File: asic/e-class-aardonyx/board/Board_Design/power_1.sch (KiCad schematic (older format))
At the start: 28 parts, among them J5 PJ-202H PWRJACK, J6 Conn_1x3_M, SW1 SW_SPST, U4 TPS54627DDAR

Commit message: update pending  footprint
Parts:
- F1: footprint Capacitor_THT:C_Disc_D9.0mm_W5.0mm_P7.50mm -> Aardonyx:vishay_ptccl_d1mm_w5mm
- SW1: footprint Button_Switch_THT:SW_NKK_G1xJP -> Aardonyx:SW_toggle_spst_2.54mm
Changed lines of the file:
@@
 EESchema Schematic File Version 4
-LIBS:Aardonyx-cache
-EELAYER 29 0
+EELAYER 30 0
 EELAYER END
 $Descr A4 11693 8268
@@
 F 0 "F1" V 4475 1600 50  0000 C CNN
 F 1 "PTCCL13H921DBE" V 4550 1700 50  0000 C CNN
-F 2 "Capacitor_THT:C_Disc_D9.0mm_W5.0mm_P7.50mm" H 4750 1400 50  0001 L CNN
+F 2 "Aardonyx:vishay_ptccl_d1mm_w5mm" H 4750 1400 50  0001 L CNN
 F 3 "https://www.digikey.in/products/en?keywords=PTCCL13H921DBE" H 4700 1600 50  0001 C CNN
 F 4 "PTC RESET FUSE 30V 920MA RADIAL" H 4700 1600 50  0001 C CNN "Description"
@@
 F 0 "SW1" H 4200 1835 50  0000 C CNN
 F 1 "SW_SPST" H 4200 1744 50  0000 C CNN
-F 2 "Button_Switch_THT:SW_NKK_G1xJP" H 4200 1600 50  0001 C CNN
+F 2 "Aardonyx:SW_toggle_spst_2.54mm" H 4200 1600 50  0001 C CNN
 F 3 "https://www.digikey.com/product-detail/en/te-connectivity-alcoswitch-switches/TMS6T1B1M1QE/450-2109-ND/5125729" H 4200 1600 50  0001 C CNN
 F 4 "SWITCH TOGGLE SPST 3A 120V" H 4200 1600 50  0001 C CNN "Description"

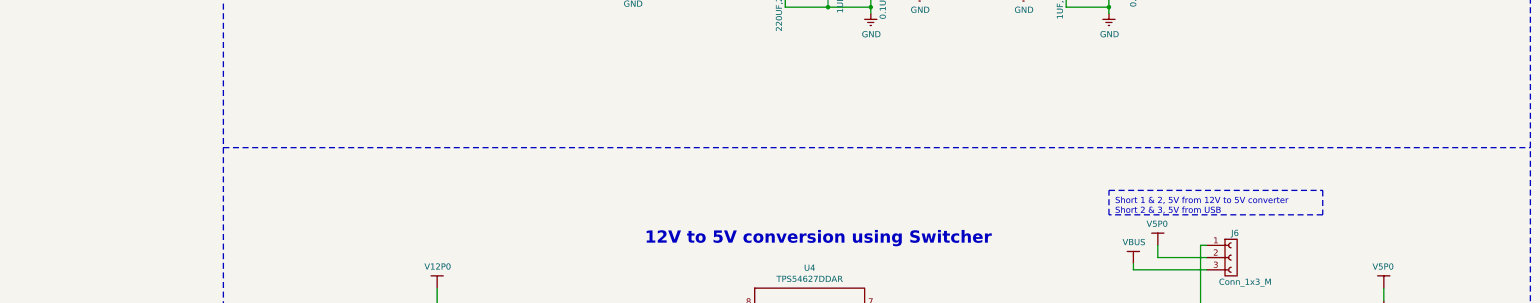
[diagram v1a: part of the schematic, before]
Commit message: update footprint & component placement
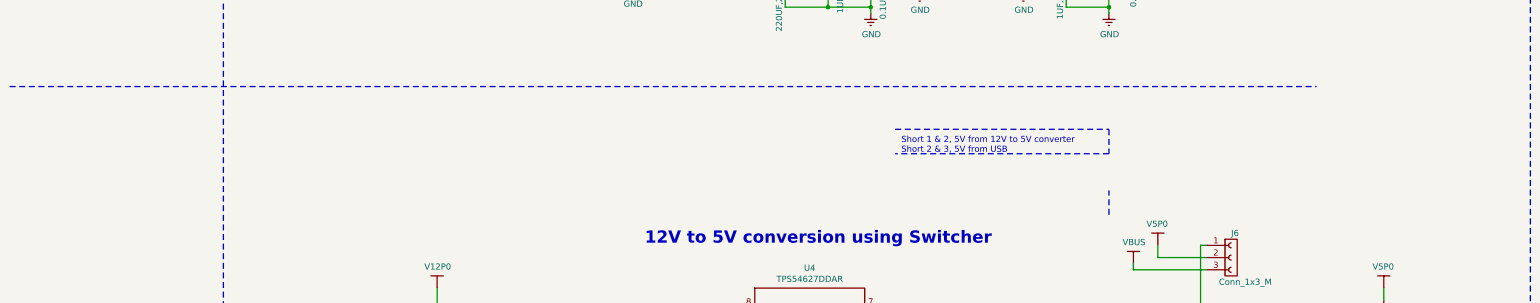
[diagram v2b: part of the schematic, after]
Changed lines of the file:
@@
 	500  7750 500  500
 Wire Notes Line
-	500  3300 11200 3300
+	-1250 2800 9450 2800
 Text Notes 3950 4100 0    100  ~ 20
 12V to 5V conversion using Switcher
@@
 	0    1    1    0
 $EndComp
-Text Notes 7800 3850 0    50   ~ 0
+Text Notes 6050 3350 0    50   ~ 0
 Short 1 & 2, 5V from 12V to 5V converter\nShort 2 & 3, 5V from USB
 $Comp
@@
 $EndComp
 Wire Notes Line
-	7750 3650 9500 3650
+	6000 3150 7750 3150
 Wire Notes Line
-	9500 3650 9500 3850
+	7750 3150 7750 3350
 Wire Notes Line
-	9500 3850 7750 3850
+	7750 3350 6000 3350
 Wire Notes Line
 	7750 3850 7750 3650

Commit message: updated compo placement
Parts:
- TP5: footprint TestPoint:TestPoint_Bridge_Pitch2.54mm_Drill0.7mm -> Connector_PinHeader_2.54mm:PinHeader_1x01_P2.54mm_Vertical
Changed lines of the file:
@@
 F 0 "TP5" V 10104 6238 50  0000 L CNN
 F 1 "TestPoint" V 10195 6238 50  0000 L CNN
-F 2 "TestPoint:TestPoint_Bridge_Pitch2.54mm_Drill0.7mm" H 10350 6050 50  0001 C CNN
+F 2 "Connector_PinHeader_2.54mm:PinHeader_1x01_P2.54mm_Vertical" H 10350 6050 50  0001 C CNN
 F 3 "" H 10350 6050 50  0001 C CNN
 	1    10150 6050

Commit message: add bom
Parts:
- C37: Maufaturer AVX Corporation -> AVX Corporation
- D3: Maufaturer Lumex Opto/Components Inc. -> Lumex Opto/Components Inc.
- L1: Description CMC 15A 2LN 60 OHM SMD -> CMC 15A 2LN 60 OHM SMD; Maufaturer Laird-Signal Integrity Products -> Laird-Signal Integrity Products
- SW1: Digikey PartNumber SWITCH TOGGLE SPST 3A 120V -> TMS6T1B1M1QE
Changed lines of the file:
@@
 F 5 "478-12518-1-ND" H 5100 1850 50  0001 C CNN "Digikey PartNumber"
 F 6 "TCN4227M025R0100" H 5100 1850 50  0001 C CNN "Manufactured Part Number"
-F 7 "	AVX Corporation" H 5100 1850 50  0001 C CNN "Maufaturer"
+F 7 "AVX Corporation" H 5100 1850 50  0001 C CNN "Maufaturer"
 	1    5100 1850
 	1    0    0    -1
@@
 F 2 "Aardonyx:L_Laird_L9.55_W2.84" H 6600 1700 50  0001 C CNN
 F 3 "https://www.digikey.com/product-detail/en/laird-signal-integrity-products/CM3421Y600R-10/240-2501-1-ND/935987" H 6600 1700 50  0001 C CNN
-F 4 "	CMC 15A 2LN 60 OHM SMD" H 6600 1700 50  0001 C CNN "Description"
+F 4 "CMC 15A 2LN 60 OHM SMD" H 6600 1700 50  0001 C CNN "Description"
 F 5 "240-2501-1-ND" H 6600 1700 50  0001 C CNN "Digikey PartNumber"
 F 6 "CM3421Y600R-10" H 6600 1700 50  0001 C CNN "Manufactured Part Number"
-F 7 "	Laird-Signal Integrity Products" H 6600 1700 50  0001 C CNN "Maufaturer"
+F 7 "Laird-Signal Integrity Products" H 6600 1700 50  0001 C CNN "Maufaturer"
 	1    6600 1700
 	1    0    0    -1
@@
 F 3 "https://www.digikey.com/product-detail/en/lumex-opto-components-inc/SML-LX1206GW-TR/67-1002-1-ND/270799" H 10000 5150 50  0001 C CNN
 F 4 "LED GREEN DIFFUSED 1206 SMD" H 10000 5150 50  0001 C CNN "Description"
-F 5 "	Lumex Opto/Components Inc." H 10000 5150 50  0001 C CNN "Maufaturer"
+F 5 "Lumex Opto/Components Inc." H 10000 5150 50  0001 C CNN "Maufaturer"
 F 6 "67-1002-1-ND" H 10000 5150 50  0001 C CNN "Digikey PartNumber"
 F 7 "SML-LX1206GW-TR" H 10000 5150 50  0001 C CNN "Manufactured Part Number"
@@
 F 3 "https://www.digikey.com/product-detail/en/te-connectivity-alcoswitch-switches/TMS6T1B1M1QE/450-2109-ND/5125729" H 4200 1600 50  0001 C CNN
 F 4 "SWITCH TOGGLE SPST 3A 120V" H 4200 1600 50  0001 C CNN "Description"
-F 5 "SWITCH TOGGLE SPST 3A 120V" H 4200 1600 50  0001 C CNN "Digikey PartNumber"
+F 5 "TMS6T1B1M1QE" H 4200 1600 50  0001 C CNN "Digikey PartNumber"
 F 6 "TMS6T1B1M1QE (2267080-1)" H 4200 1600 50  0001 C CNN "Manufactured Part Number"
 F 7 "TE Connectivity ALCOSWITCH Switches" H 4200 1600 50  0001 C CNN "Maufaturer"

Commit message: Updated few components
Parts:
- L2: Description FIXED IND 3.3UH 6.6A 17 MOHM SMD -> FIXED IND 3.3UH 6.6A 15 MOHM SMD; Digikey PartNumber 732-6781-2-ND -> SRN8040TA-3R3YCT-ND; Manufactured Part Number 78477033 -> SRN8040TA-3R3Y; Maufaturer Wurth Elektronik -> Bourns Inc.
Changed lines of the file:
@@
 EESchema Schematic File Version 4
-EELAYER 30 0
+LIBS:Aardonyx-cache
+EELAYER 29 0
 EELAYER END
 $Descr A4 11693 8268
@@
 F 1 "3.3UH" V 6600 4900 50  0000 C CNN
 F 2 "Inductor_SMD:L_Wuerth_WE-PD-Typ-LS" H 6650 4900 50  0001 C CNN
-F 3 "https://www.digikey.com/product-detail/en/w%C3%BCrth-elektronik/78477033/732-6781-2-ND/5168775" H 6650 4900 50  0001 C CNN
-F 4 "FIXED IND 3.3UH 6.6A 17 MOHM SMD" H 6650 4900 50  0001 C CNN "Description"
-F 5 "732-6781-2-ND" H 6650 4900 50  0001 C CNN "Digikey PartNumber"
-F 6 "78477033" H 6650 4900 50  0001 C CNN "Manufactured Part Number"
-F 7 "Wurth Elektronik" H 6650 4900 50  0001 C CNN "Maufaturer"
+F 3 "https://www.digikey.in/product-detail/en/bourns-inc/SRN8040TA-3R3Y/SRN8040TA-3R3YCT-ND/6155255" H 6650 4900 50  0001 C CNN
+F 4 "	FIXED IND 3.3UH 6.6A 15 MOHM SMD" H 6650 4900 50  0001 C CNN "Description"
+F 5 "SRN8040TA-3R3YCT-ND" H 6650 4900 50  0001 C CNN "Digikey PartNumber"
+F 6 "	SRN8040TA-3R3Y" H 6650 4900 50  0001 C CNN "Manufactured Part Number"
+F 7 "Bourns Inc." H 6650 4900 50  0001 C CNN "Maufaturer"
 	1    6650 4900
 	0    -1   -1   0

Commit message: update footprint & bom
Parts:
- L2: footprint Inductor_SMD:L_Wuerth_WE-PD-Typ-LS -> Aardonyx:Bourns_srn8040ta_L8.5_W6.6; Description FIXED IND 3.3UH 6.6A 15 MOHM SMD -> FIXED IND 3.3UH 6.6A 15 MOHM SMD; Manufactured Part Number SRN8040TA-3R3Y -> SRN8040TA-3R3Y
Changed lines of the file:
@@
 EESchema Schematic File Version 4
-LIBS:Aardonyx-cache
-EELAYER 29 0
+EELAYER 30 0
 EELAYER END
 $Descr A4 11693 8268
@@
 F 0 "L2" V 6700 5050 50  0000 C CNN
 F 1 "3.3UH" V 6600 4900 50  0000 C CNN
-F 2 "Inductor_SMD:L_Wuerth_WE-PD-Typ-LS" H 6650 4900 50  0001 C CNN
+F 2 "Aardonyx:Bourns_srn8040ta_L8.5_W6.6" H 6650 4900 50  0001 C CNN
 F 3 "https://www.digikey.in/product-detail/en/bourns-inc/SRN8040TA-3R3Y/SRN8040TA-3R3YCT-ND/6155255" H 6650 4900 50  0001 C CNN
-F 4 "	FIXED IND 3.3UH 6.6A 15 MOHM SMD" H 6650 4900 50  0001 C CNN "Description"
+F 4 "FIXED IND 3.3UH 6.6A 15 MOHM SMD" H 6650 4900 50  0001 C CNN "Description"
 F 5 "SRN8040TA-3R3YCT-ND" H 6650 4900 50  0001 C CNN "Digikey PartNumber"
-F 6 "	SRN8040TA-3R3Y" H 6650 4900 50  0001 C CNN "Manufactured Part Number"
+F 6 "SRN8040TA-3R3Y" H 6650 4900 50  0001 C CNN "Manufactured Part Number"
 F 7 "Bourns Inc." H 6650 4900 50  0001 C CNN "Maufaturer"
 	1    6650 4900
